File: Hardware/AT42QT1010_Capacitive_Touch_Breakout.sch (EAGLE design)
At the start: 24 parts, among them Q1 NPN, U1 AT42QT1010SOT23

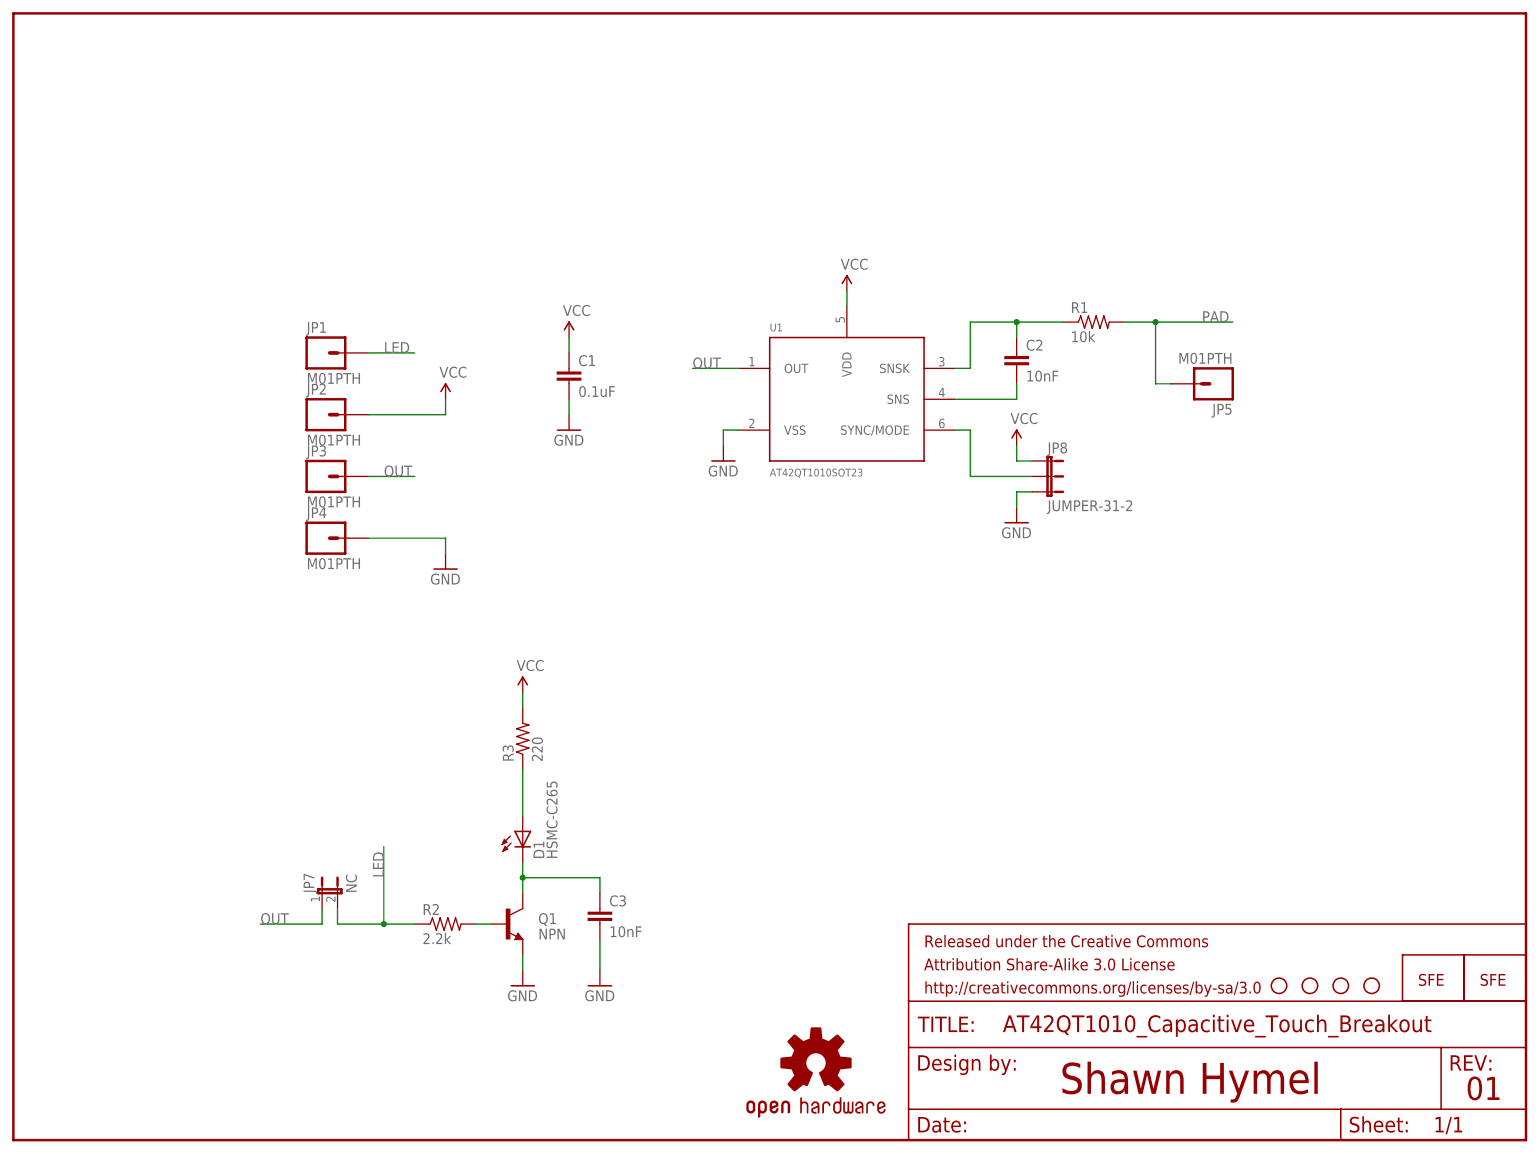
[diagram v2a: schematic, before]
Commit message: Fixed issues from design review
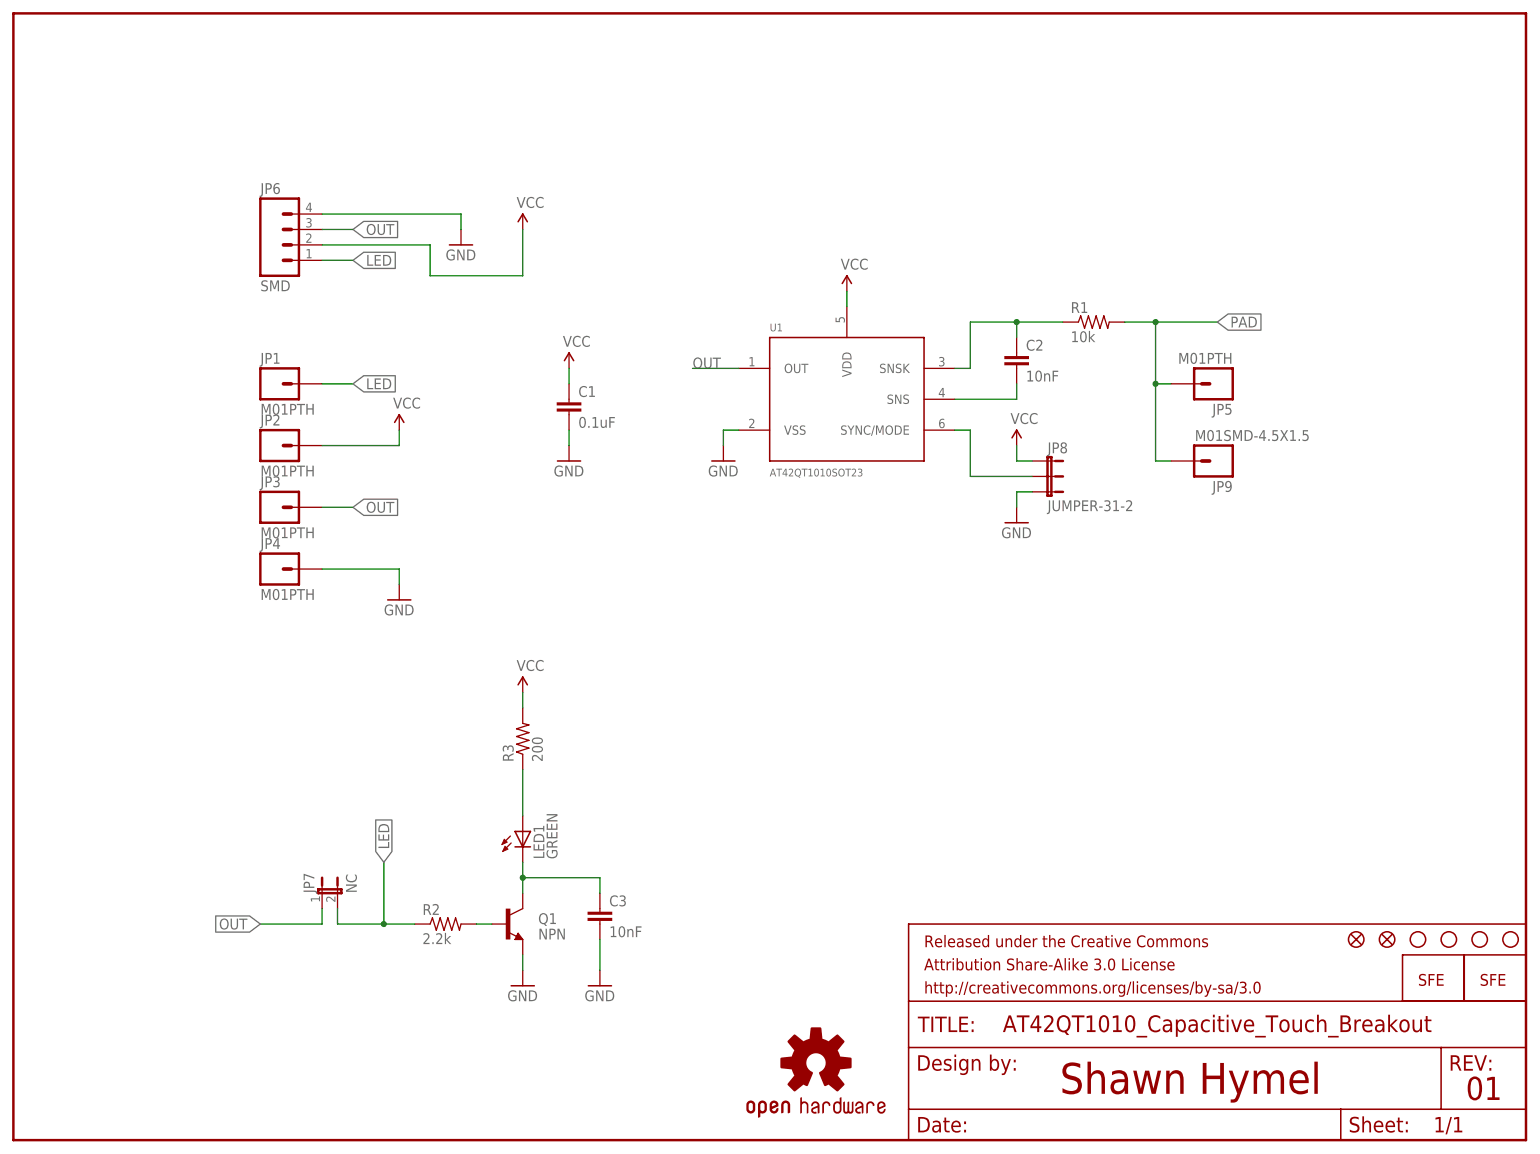
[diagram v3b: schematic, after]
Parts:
- removed D1: HSMC-C265, SparkFun-LED:HSMC-C265
- added FID1, FID2: FIDUCIAL1X2, SparkFun-Aesthetics:FIDUCIAL1X2
- added JP6: SMD, SparkFun-Connectors:M04SMD
- added JP9: M01SMD-4.5X1.5, SparkFun-Connectors:M01SMD-4.5X1.5
- added LED1: GREEN, SparkFun-LED:LED1206-BOTTOM
- R3: value 220 -> 200
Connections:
- net GND: now also JP6.4
- net LED: now also JP6.1
- net N$11: now also LED1.C; no longer D1.C
- net N$12: now also LED1.A; no longer D1.A
- net OUT: now also JP6.3
- net PAD: now also JP9.1
- net VCC: now also JP6.2
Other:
- moved on the sheet: C1, JP1, JP2, JP3, JP4
